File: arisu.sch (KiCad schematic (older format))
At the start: 40 parts, among them J1 USB_B_Micro, J10 PF6, J11 PF7, J12 VCC, J13 D+, J14 D-, J15 GND, J2 MISO, J3 VCC, J4 SCK, J5 MOSI, J6 RES, J7 GND, J8 PF4, J9 PF5, U1 USBLC6-2SC6, U2 ATmega32U4-AU, Y1 Crystal_GND24

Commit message: Initial Commit
Initial Commit
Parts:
- J1: symbol Connector:USB_B_Micro -> arisu-rescue:USB_B_Micro-Connector
- U1: symbol Power_Protection:USBLC6-2SC6 -> arisu-rescue:USBLC6-2SC6-Power_Protection
- U2: symbol MCU_Microchip_ATmega:ATmega32U4-AU -> arisu-rescue:ATmega32U4-AU-MCU_Microchip_ATmega
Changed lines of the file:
@@
 EESchema Schematic File Version 4
+LIBS:arisu-cache
 EELAYER 30 0
 EELAYER END
@@
 $EndDescr
 $Comp
-L MCU_Microchip_ATmega:ATmega32U4-AU U2
+L arisu-rescue:ATmega32U4-AU-MCU_Microchip_ATmega U2
 U 1 1 5C4B1F82
 P 4500 4250
@@
 $EndComp
 $Comp
-L Connector:USB_B_Micro J1
+L arisu-rescue:USB_B_Micro-Connector J1
 U 1 1 5C4B21E5
 P 1000 4800
@@
 $EndComp
 $Comp
-L Power_Protection:USBLC6-2SC6 U1
+L arisu-rescue:USBLC6-2SC6-Power_Protection U1
 U 1 1 5C4B2347
 P 1900 5650

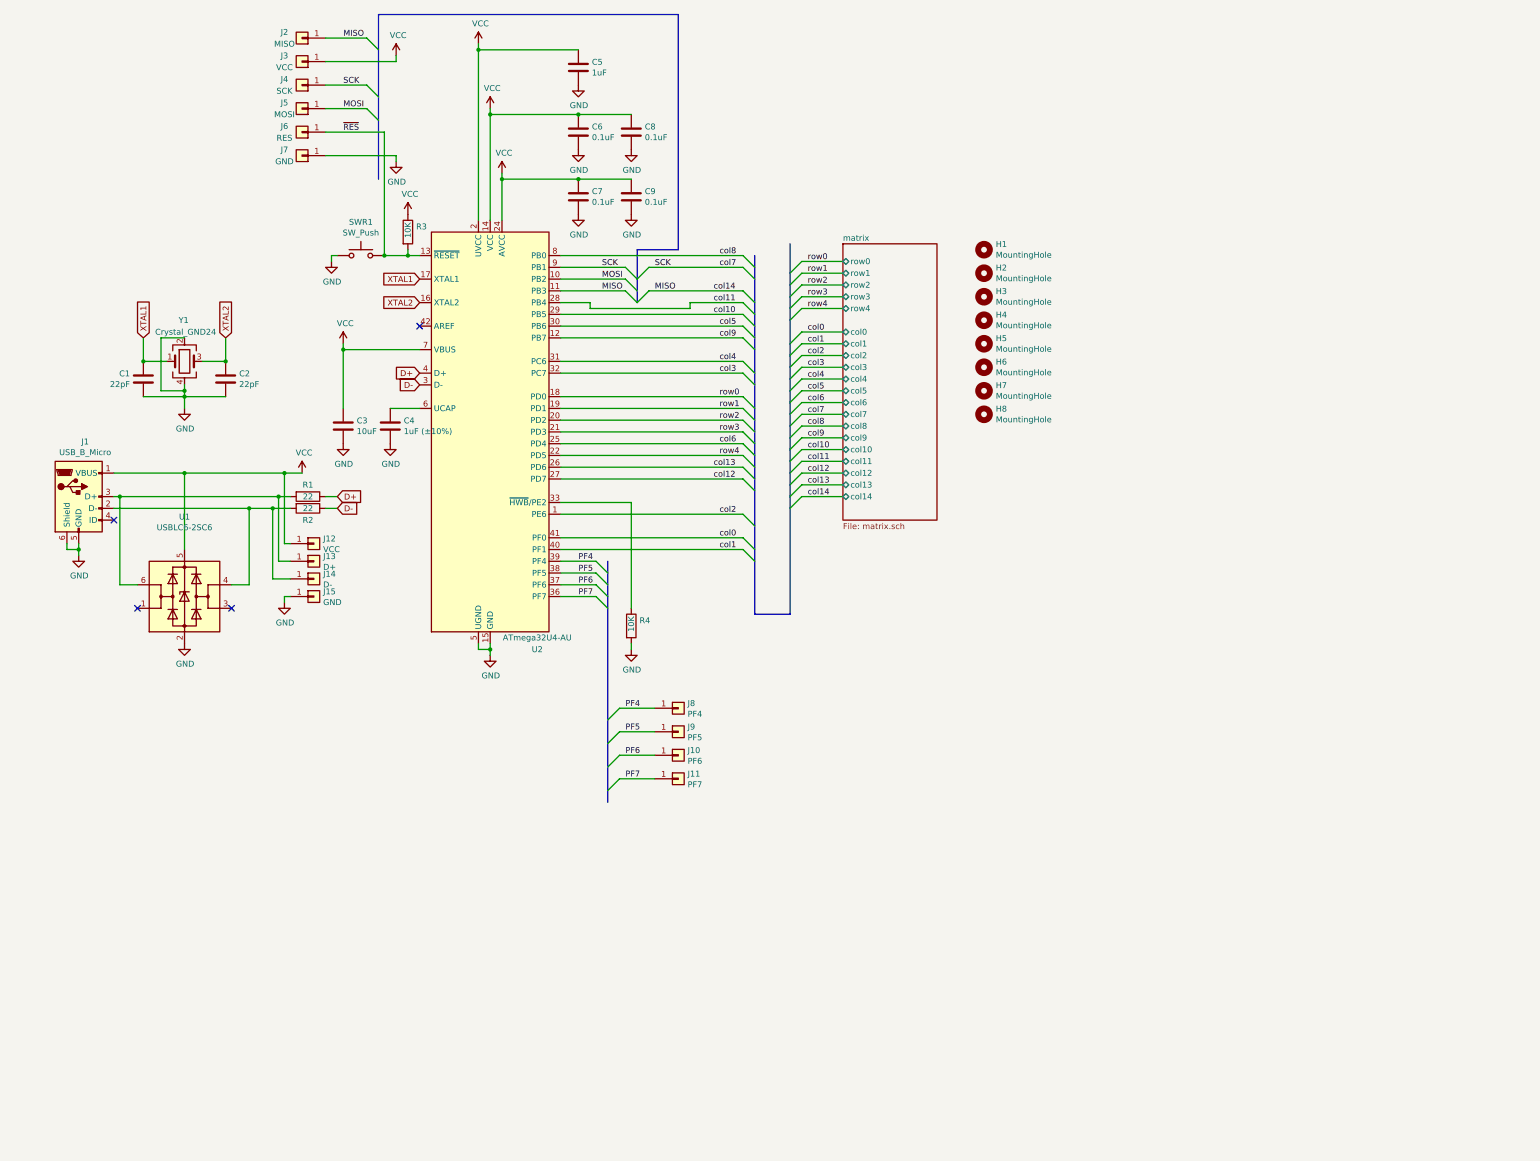
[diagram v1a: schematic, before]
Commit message: Add hotswap and USB-C
Add hotswap and USB-C
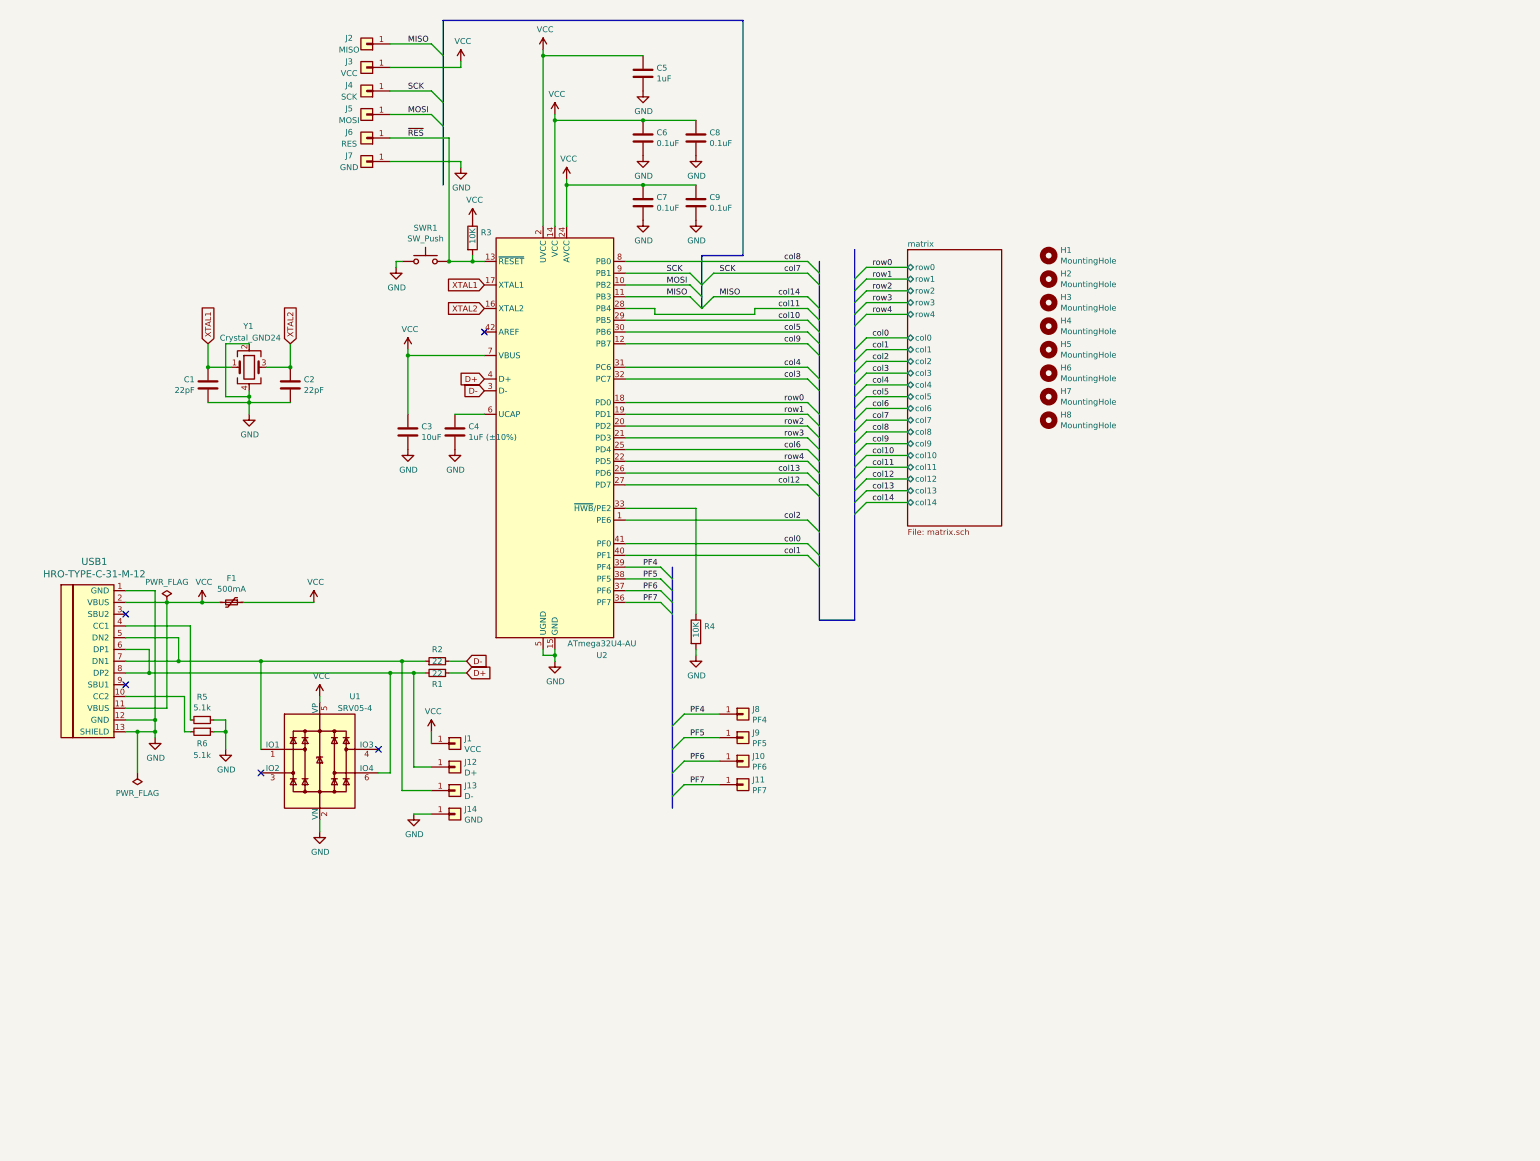
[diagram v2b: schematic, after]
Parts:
- removed J1: USB_B_Micro, Connectors_USB:USB_Micro-B_Molex-105017-0001, symbol arisu-rescue:USB_B_Micro-Connector
- removed J15: GND, Pin_Headers:Pin_Header_Straight_1x01_Pitch2.54mm, symbol Connector_Generic:Conn_01x01
- removed R1, R2: 22, Resistors_SMD:R_0805_HandSoldering, symbol Device:R
- removed U1: USBLC6-2SC6, TO_SOT_Packages_SMD:SOT-23-6_Handsoldering, symbol arisu-rescue:USBLC6-2SC6-Power_Protection
- added F1: 500mA, Fuse:Fuse_1206_3216Metric_Pad1.42x1.75mm_HandSolder, symbol Device:Polyfuse_Small
- added J1: VCC, Connector_PinHeader_2.54mm:PinHeader_1x01_P2.54mm_Vertical, symbol Connector_Generic:Conn_01x01
- added R1, R2: 22, Resistor_SMD:R_0805_2012Metric_Pad1.20x1.40mm_HandSolder, symbol Device:R_Small
- added R5, R6: 5.1k, Resistor_SMD:R_0805_2012Metric_Pad1.20x1.40mm_HandSolder, symbol Device:R_Small
- added U1: SRV05-4, Package_TO_SOT_SMD:SOT-23-6, symbol Power_Protection:SRV05-4
- added USB1: HRO-TYPE-C-31-M-12, Type-C:HRO-TYPE-C-31-M-12-HandSoldering, symbol Type-C:HRO-TYPE-C-31-M-12
- J10, J11, J2, J3, J4, J5, J6, J7, J8, J9: footprint Pin_Headers:Pin_Header_Straight_1x01_Pitch2.54mm -> Connector_PinHeader_2.54mm:PinHeader_1x01_P2.54mm_Vertical
- J12: value VCC -> D+; footprint Pin_Headers:Pin_Header_Straight_1x01_Pitch2.54mm -> Connector_PinHeader_2.54mm:PinHeader_1x01_P2.54mm_Vertical
- J13: value D+ -> D-; footprint Pin_Headers:Pin_Header_Straight_1x01_Pitch2.54mm -> Connector_PinHeader_2.54mm:PinHeader_1x01_P2.54mm_Vertical
- J14: value D- -> GND; footprint Pin_Headers:Pin_Header_Straight_1x01_Pitch2.54mm -> Connector_PinHeader_2.54mm:PinHeader_1x01_P2.54mm_Vertical
- R3, R4: footprint Resistors_SMD:R_0805_HandSoldering -> Resistor_SMD:R_0805_2012Metric_Pad1.20x1.40mm_HandSolder
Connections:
- net D+: now also R2.1
- net D-: now also R1.2
- net GND: now also J14.1 (Pin_1), R5.1, R6.1, U1.2 (VN), USB1.1 (GND), USB1.12 (GND), USB1.13 (SHIELD)
- net VCC: now also F1.1, F1.2, J1.1 (Pin_1), U1.5 (VP), USB1.11 (VBUS), USB1.2 (VBUS); no longer J12.1 (Pin_1)
- net at J13.1 (Pin_1): now also R1.1, U1.1 (IO1), USB1.5 (DN2), USB1.7 (DN1)
- new net: R6.2, USB1.10 (CC2)
- new net: R5.2, USB1.4 (CC1)
- new net: J12.1 (Pin_1), R2.2, U1.6 (IO4), USB1.6 (DP1), USB1.8 (DP2)
- no-connect marks 4 -> 5
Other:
- moved on the sheet: C1, C2, C3, C4, C5, C6, C7, C8, C9, H1, H2, H3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

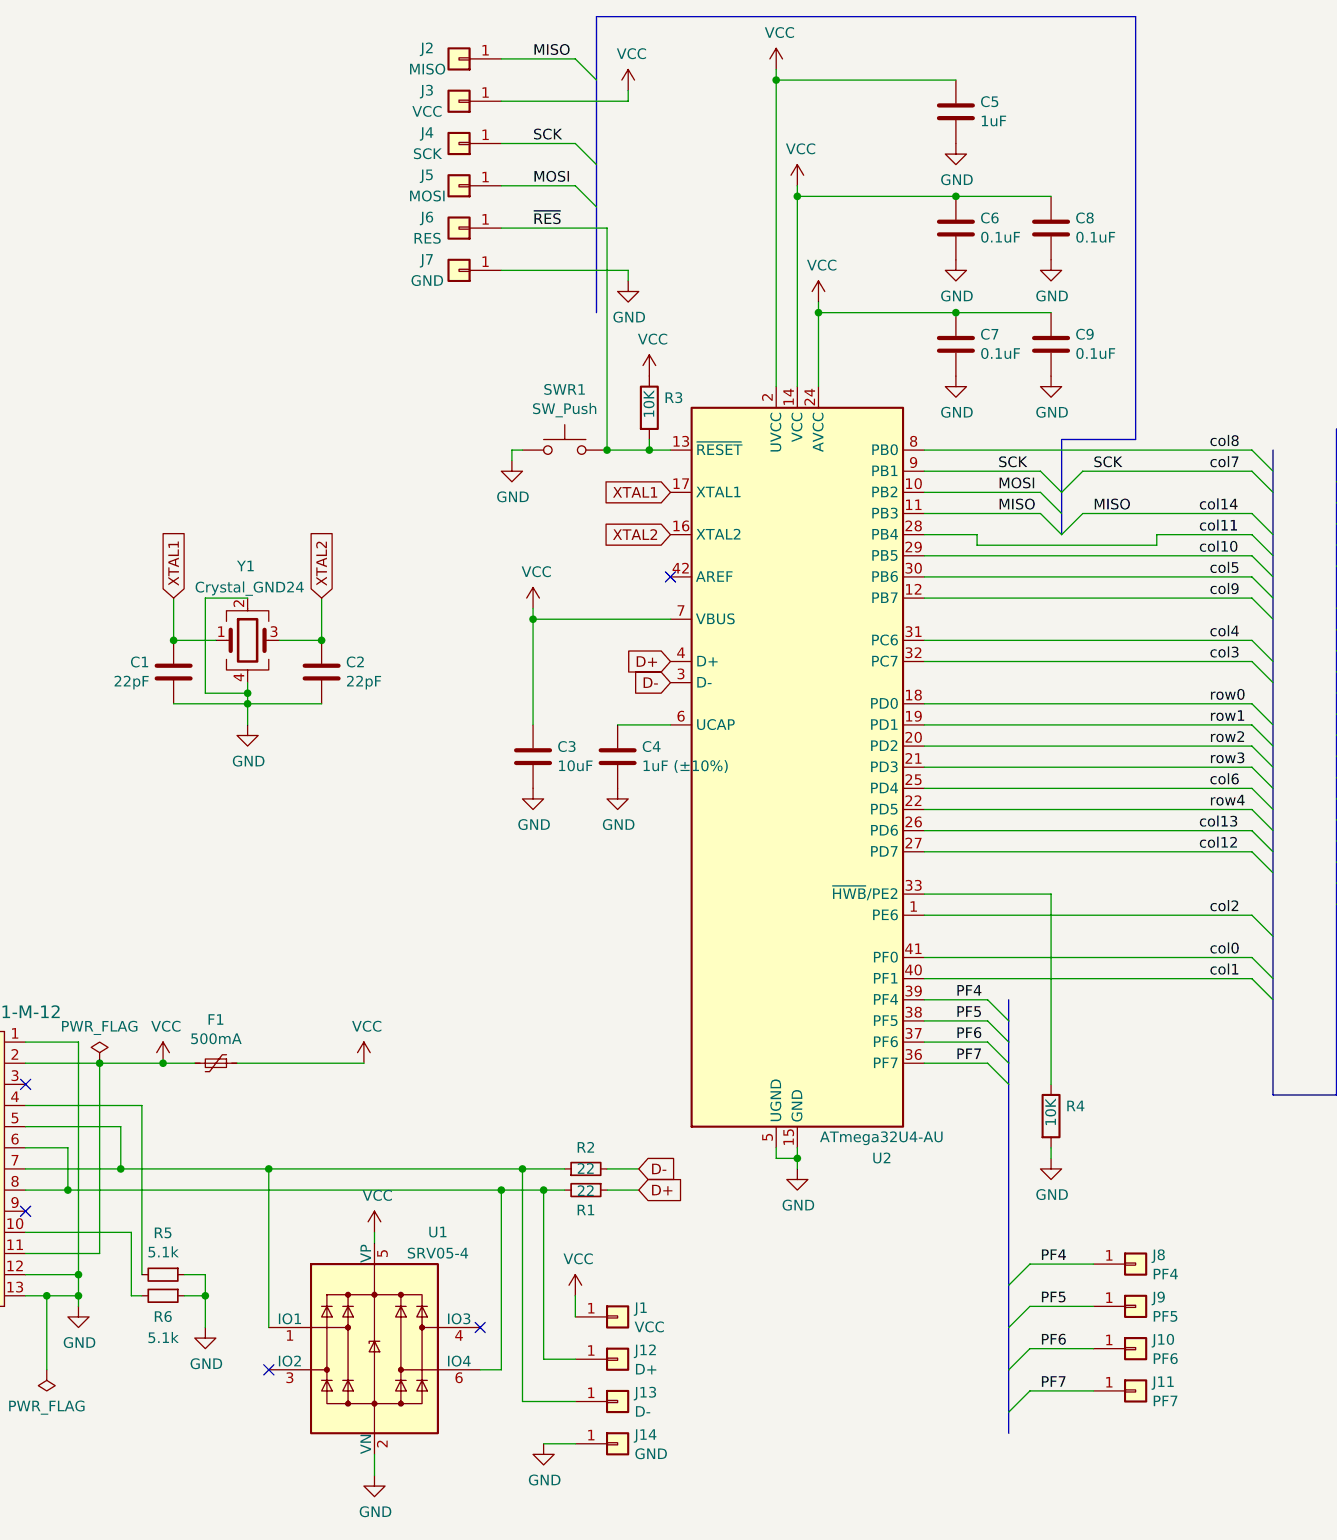
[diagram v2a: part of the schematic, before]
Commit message: Update footprints
Update backspace to 2U, left spacebar to 2.25U, left Alt to 1.25U
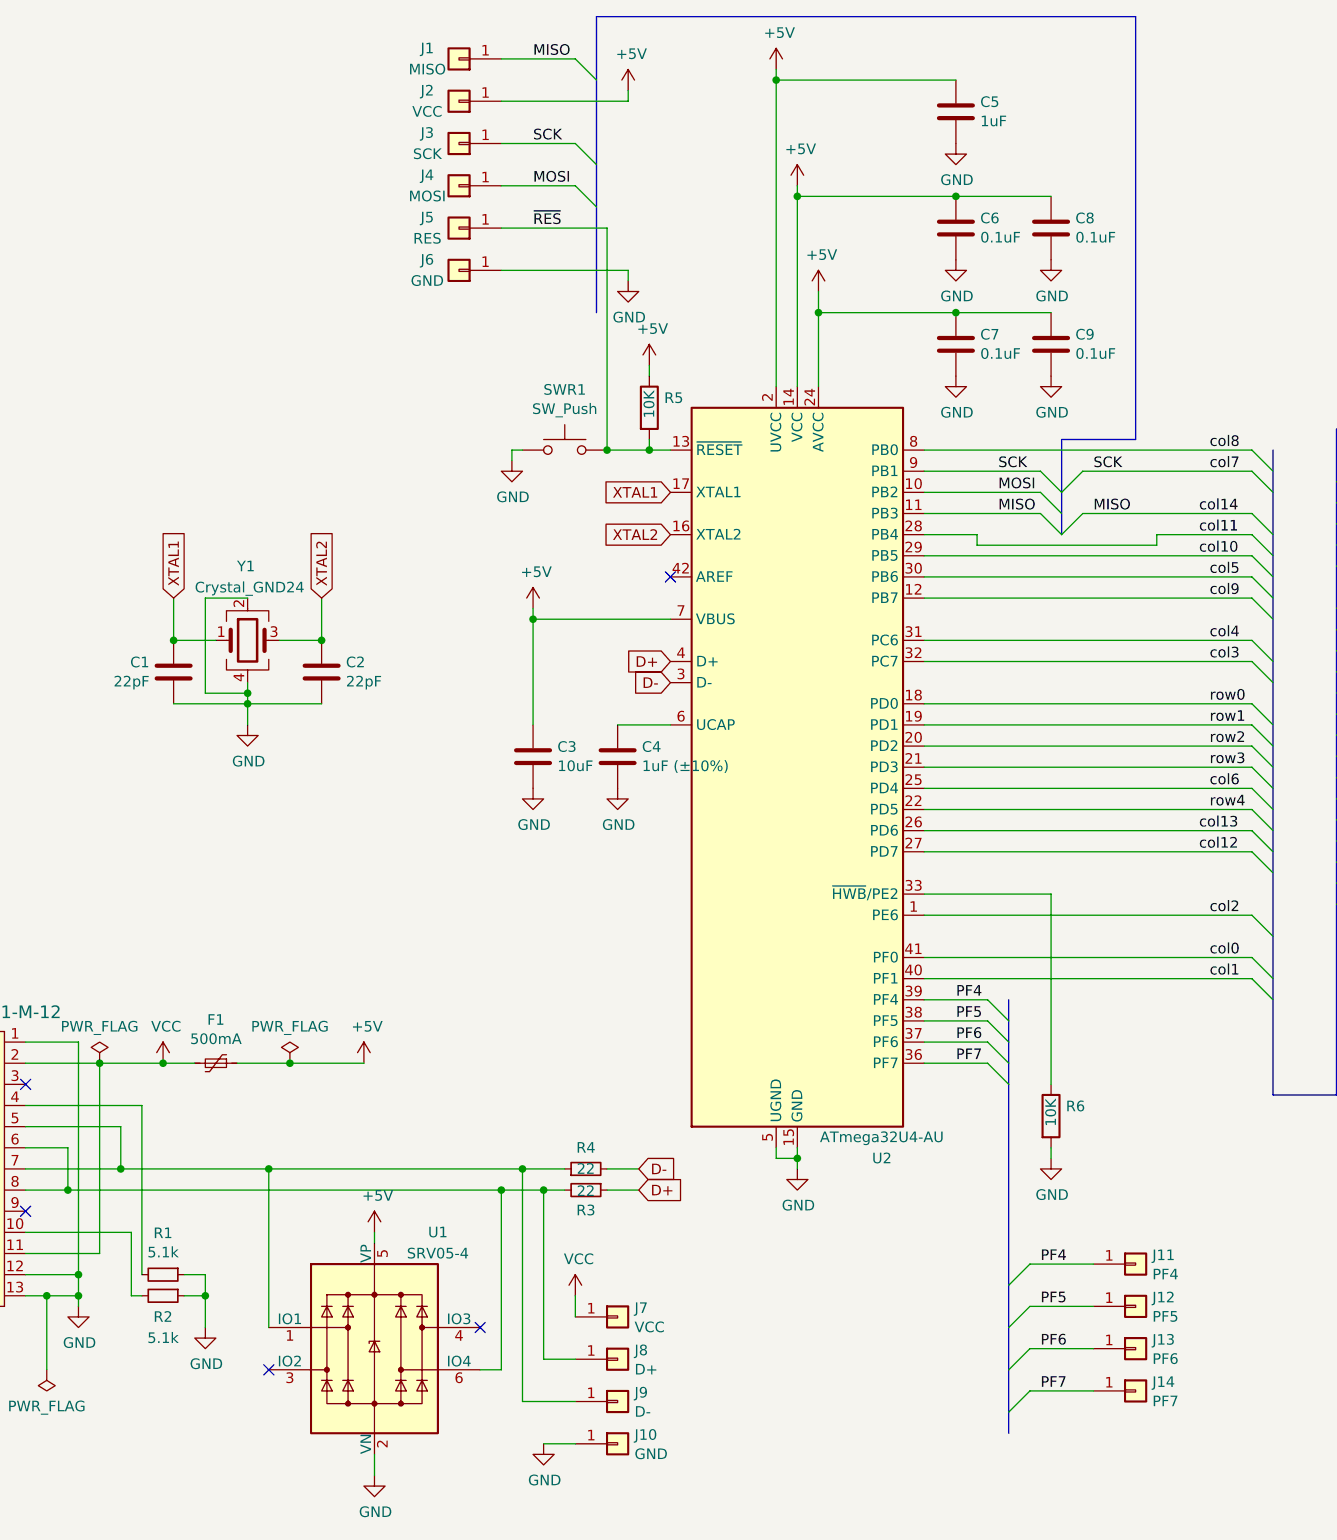
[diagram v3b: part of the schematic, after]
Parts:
- renumbered J2 to J1, J14 to J10, J8 to J11, J9 to J12, J10 to J13, J11 to J14, J3 to J2, J4 to J3, J5 to J4, J6 to J5, J7 to J6, J1 to J7, J12 to J8, J13 to J9, R5 to R1, R6 to R2, R1 to R3, R2 to R4, R3 to R5, R4 to R6
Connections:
- net VCC: no longer C3.1, C5.1, C6.1, C7.1, C8.1, C9.1, F1.1, J2.1 (Pin_1), R5.1, U1.5 (VP), U2.14 (VCC), U2.2 (UVCC), U2.24 (AVCC), U2.34 (VCC), U2.44 (AVCC), U2.7 (VBUS)
- new net +5V: C3.1, C5.1, C6.1, C7.1, C8.1, C9.1, F1.1, J2.1 (Pin_1), R5.1, U1.5 (VP), U2.14 (VCC), U2.2 (UVCC), U2.24 (AVCC), U2.34 (VCC), U2.44 (AVCC), U2.7 (VBUS)

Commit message: RGB in Progress
RGB in Progress
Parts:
- removed J14: PF7, Connector_PinHeader_2.54mm:PinHeader_1x01_P2.54mm_Vertical, symbol Connector_Generic:Conn_01x01
- added C10, C11, C12, C13, C14, C15, C16, C17, C18, C19, C20, C21, C22, C23: 0.1uF, Capacitor_SMD:C_0805_2012Metric_Pad1.18x1.45mm_HandSolder, symbol Device:C_Small
- added R7: 510, Resistor_SMD:R_0805_2012Metric_Pad1.20x1.40mm_HandSolder, symbol Device:R_Small
- added RGB1, RGB10, RGB11, RGB12, RGB13, RGB14, RGB2, RGB3, RGB4, RGB5, RGB6, RGB7, RGB8, RGB9: WS2812B, LED_SMD:LED_WS2812B_PLCC4_5.0x5.0mm_P3.2mm, symbol LED:WS2812B
- C1, C2, C3, C4, C5, C6, C7, C8, C9: footprint Capacitors_SMD:C_0805_HandSoldering -> Capacitor_SMD:C_0805_2012Metric_Pad1.18x1.45mm_HandSolder
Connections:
- net +5V: now also C10.1, C11.1, C12.1, C13.1, C14.1, C15.1, C16.1, C17.1, C18.1, C19.1, C20.1, C21.1, C22.1, C23.1, RGB1.1 (VDD), RGB10.1 (VDD), RGB11.1 (VDD), RGB12.1 (VDD), RGB13.1 (VDD), RGB14.1 (VDD), RGB2.1 (VDD), RGB3.1 (VDD), RGB4.1 (VDD), RGB5.1 (VDD), RGB6.1 (VDD), RGB7.1 (VDD), RGB8.1 (VDD), RGB9.1 (VDD)
- net GND: now also C10.2, C11.2, C12.2, C13.2, C14.2, C15.2, C16.2, C17.2, C18.2, C19.2, C20.2, C21.2, C22.2, C23.2, RGB1.3 (VSS), RGB10.3 (VSS), RGB11.3 (VSS), RGB12.3 (VSS), RGB13.3 (VSS), RGB14.3 (VSS), RGB2.3 (VSS), RGB3.3 (VSS), RGB4.3 (VSS), RGB5.3 (VSS), RGB6.3 (VSS), RGB7.3 (VSS), RGB8.3 (VSS), RGB9.3 (VSS)
- net PF7 renamed RGB
- net RGB: now also R7.1
- new net: RGB1.2 (DOUT), RGB3.4 (DIN)
- new net: R7.2, RGB1.4 (DIN)
- new net: RGB3.2 (DOUT), RGB5.4 (DIN)
- new net: RGB5.2 (DOUT), RGB7.4 (DIN)
- new net: RGB7.2 (DOUT), RGB9.4 (DIN)
- new net: RGB11.4 (DIN), RGB9.2 (DOUT)
- new net: RGB11.2 (DOUT), RGB13.4 (DIN)
- new net: RGB13.2 (DOUT), RGB2.4 (DIN)
- new net: RGB2.2 (DOUT), RGB4.4 (DIN)
- new net: RGB4.2 (DOUT), RGB6.4 (DIN)
- new net: RGB6.2 (DOUT), RGB8.4 (DIN)
- new net: RGB10.4 (DIN), RGB8.2 (DOUT)
- new net: RGB10.2 (DOUT), RGB12.4 (DIN)
- new net: RGB12.2 (DOUT), RGB14.4 (DIN)
- no-connect marks 5 -> 6
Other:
- moved on the sheet: C1, C2, C3, C4, C5, C6, C7, C8, C9, F1, H1, H2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
